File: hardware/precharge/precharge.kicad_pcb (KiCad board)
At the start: 2 copper layers, 111.8 x 81.3 mm, 109 parts, among them J1 Conn_01x02, J2 Conn_01x01, J3 Conn_01x02, J4 Conn_01x04, J5 Conn_01x03, J6 Conn_01x06, K2 G5Q-1EU DC12, K3 G5Q-1EU DC12, Q1 BC856, Q2 BC856, Q3 BC856, Q4 BC846, Q6 XP262N7002TR-G, Q7 XP262N7002TR-G, Q8 XP262N7002TR-G, U1 140817141410, U2 140817141410, U3 140817141410, U4 TLV274, U5 40106, U7 4013, U8 4071, U9 4013

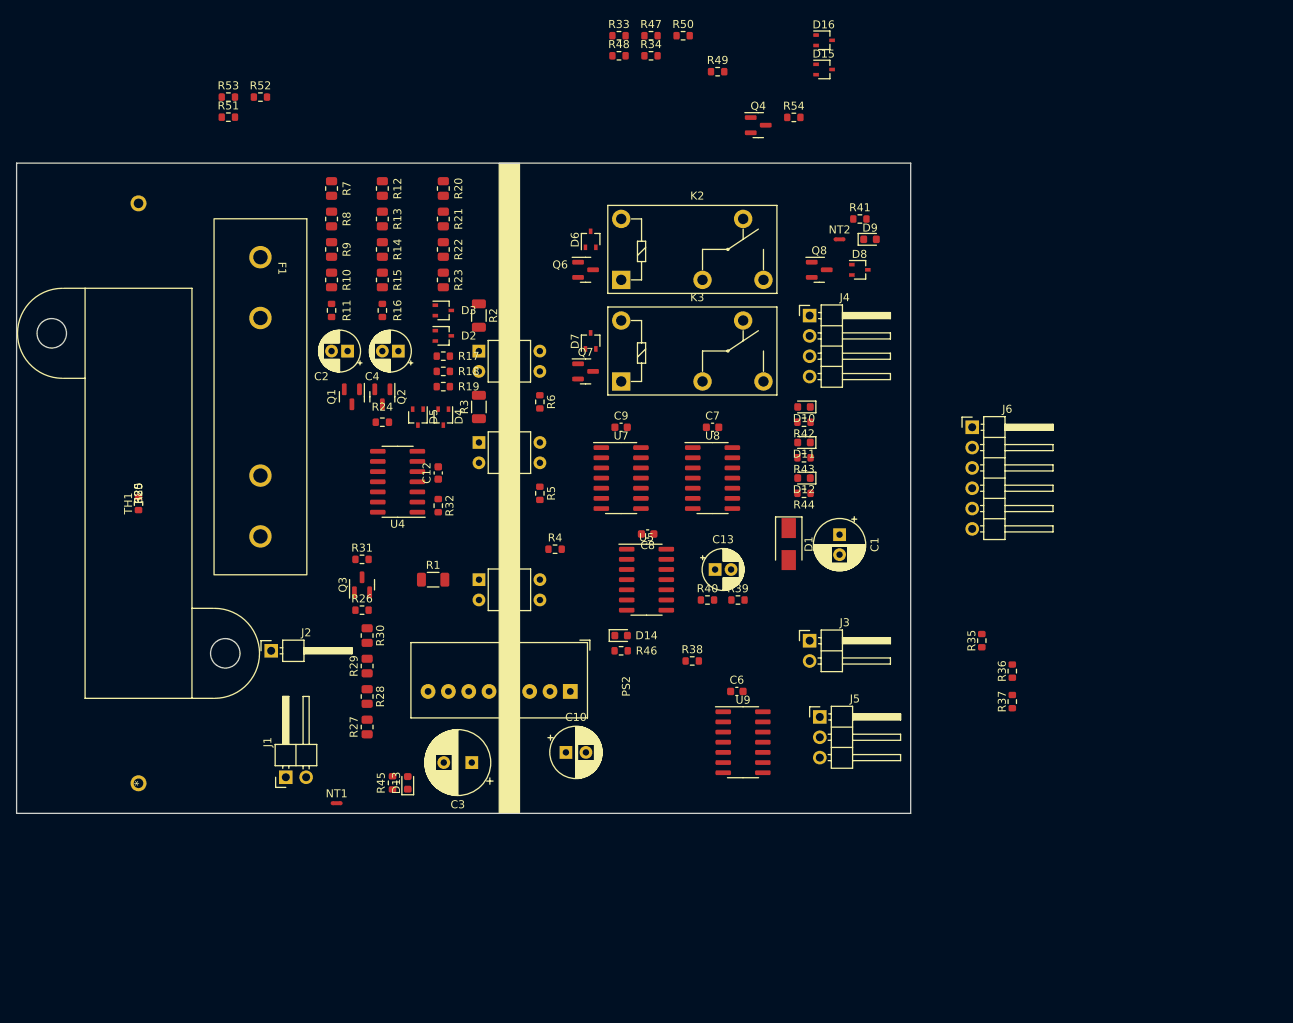
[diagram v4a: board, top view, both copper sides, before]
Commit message: Restarted PCB layout
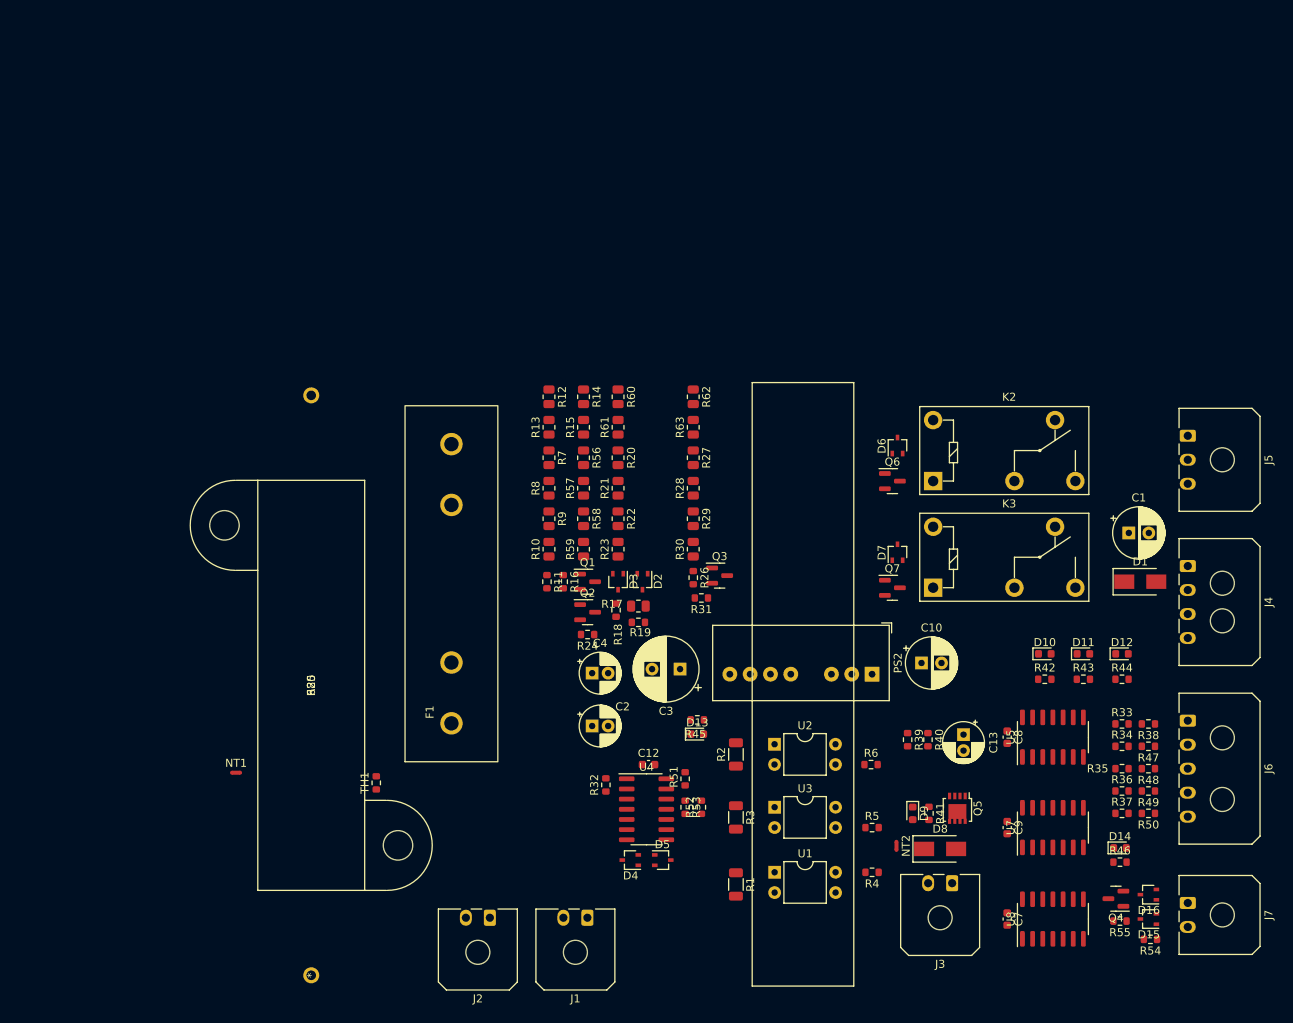
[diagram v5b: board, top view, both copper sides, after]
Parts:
- removed C6: 100n, Capacitor_SMD:C_0603_1608Metric
- removed Q8: XP262N7002TR-G, Package_TO_SOT_SMD:SOT-23
- removed U9: 4013, Package_SO:SOIC-14_3.9x8.7mm_P1.27mm
- added J7: Conn_01x02, Connector_Molex:Molex_Micro-Fit_3.0_43650-0200_1x02_P3.00mm_Horizontal, F.Cu at (256.9, 125.5)
- added Q5: BUK7M9R5-40H, Package_TO_SOT_SMD:LFPAK33, F.Cu at (228.1, 113.7)
- added R55: 10k, Resistor_SMD:R_0603_1608Metric, F.Cu at (248.4, 127.8)
- added R56: 453k, Resistor_SMD:R_0805_2012Metric, F.Cu at (181.4, 69.8)
- added R57: 453k, Resistor_SMD:R_0805_2012Metric, F.Cu at (181.4, 73.7)
- added R58: 453k, Resistor_SMD:R_0805_2012Metric, F.Cu at (181.4, 77.5)
- added R59: 453k, Resistor_SMD:R_0805_2012Metric, F.Cu at (181.4, 81.3)
- added R60: 453k, Resistor_SMD:R_0805_2012Metric, F.Cu at (185.7, 62.2)
- added R61: 453k, Resistor_SMD:R_0805_2012Metric, F.Cu at (185.7, 66.0)
- added R62: 453k, Resistor_SMD:R_0805_2012Metric, F.Cu at (195.1, 62.2)
- added R63: 453k, Resistor_SMD:R_0805_2012Metric, F.Cu at (195.1, 66.0)
- D8: value BAT54W -> SS14+; footprint Package_TO_SOT_SMD:SOT-323_SC-70 -> Diode_SMD:D_SMA
- J1, J3: footprint Connector_PinHeader_2.54mm:PinHeader_1x02_P2.54mm_Horizontal -> Connector_Molex:Molex_Micro-Fit_3.0_43650-0200_1x02_P3.00mm_Horizontal
- J2: value Conn_01x01 -> Conn_01x02; footprint Connector_PinHeader_2.54mm:PinHeader_1x01_P2.54mm_Horizontal -> Connector_Molex:Molex_Micro-Fit_3.0_43650-0200_1x02_P3.00mm_Horizontal
- J4: footprint Connector_PinHeader_2.54mm:PinHeader_1x04_P2.54mm_Horizontal -> Connector_Molex:Molex_Micro-Fit_3.0_43650-0400_1x04_P3.00mm_Horizontal
- J5: footprint Connector_PinHeader_2.54mm:PinHeader_1x03_P2.54mm_Horizontal -> Connector_Molex:Molex_Micro-Fit_3.0_43650-0300_1x03_P3.00mm_Horizontal
- J6: value Conn_01x06 -> Conn_01x05; footprint Connector_PinHeader_2.54mm:PinHeader_1x06_P2.54mm_Horizontal -> Connector_Molex:Molex_Micro-Fit_3.0_43650-0500_1x05_P3.00mm_Horizontal
- R10, R12, R13, R14, R15, R20, R21, R22, R27, R28, R29, R30, R7, R8, R9: value 680k -> 453k
- R17: value 120k -> 105k; footprint Resistor_SMD:R_0603_1608Metric -> Resistor_SMD:R_0805_2012Metric
- R18: value 1.5k -> 82
- R19: value 30k -> 31.6k
- R23: value 560k -> 348k
- moved D16 114.2 mm to (252.0, 124.5), turned to 180 degrees
- moved D15 113.7 mm to (252.0, 127.5), turned to 180 degrees
- moved R50 113.3 mm to (252.0, 114.3), turned to 180 degrees
- moved R54 112.0 mm to (252.2, 130.0), turned to 180 degrees
- moved R48 111.0 mm to (252.0, 108.7), turned to 180 degrees
- moved R47 108.4 mm to (252.0, 105.9), turned to 180 degrees
- moved R33 106.6 mm to (248.7, 103.1)
- moved Q4 106.5 mm to (247.9, 125.0), turned to 180 degrees
- moved R53 105.5 mm to (194.1, 113.5), turned to -90 degrees
- moved R49 104.8 mm to (252.0, 111.5), turned to 180 degrees
- moved R52 104.5 mm to (196.1, 113.5), turned to 90 degrees
- moved R34 104.5 mm to (248.7, 105.9)
- moved R51 100.5 mm to (194.1, 110.0), turned to -90 degrees
- moved NT2 76.2 mm to (220.5, 118.4), turned to -90 degrees
- moved R41 74.8 mm to (224.5, 114.3), turned to -90 degrees
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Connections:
- D8 pad 1: /RELAY- -> /LV side/RELAY+
- D8 pad 2: unconnected-(D8-Pad2) -> /LV side/RELAY-
- J3 pad 1: /RELAY- -> /LV side/RELAY-
- J5 pad 1: /RELAY- -> /LV side/PRECHARGE_ENABLED
- R14 pad 1: Net-(R13-Pad1) -> /HV side/HV_IN
- R15 pad 1: Net-(C4-Pad1) -> Net-(R15-Pad1)
- R20 pad 1: /HV side/HV_IN -> Net-(R20-Pad1)
- R27 pad 1: /HV side/TS+ -> Net-(R27-Pad1)
- R41 pad 2: /RELAY- -> /LV side/RELAY-
- R7 pad 1: /HV side/HV_IN -> Net-(R13-Pad1)
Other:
- board outline removed

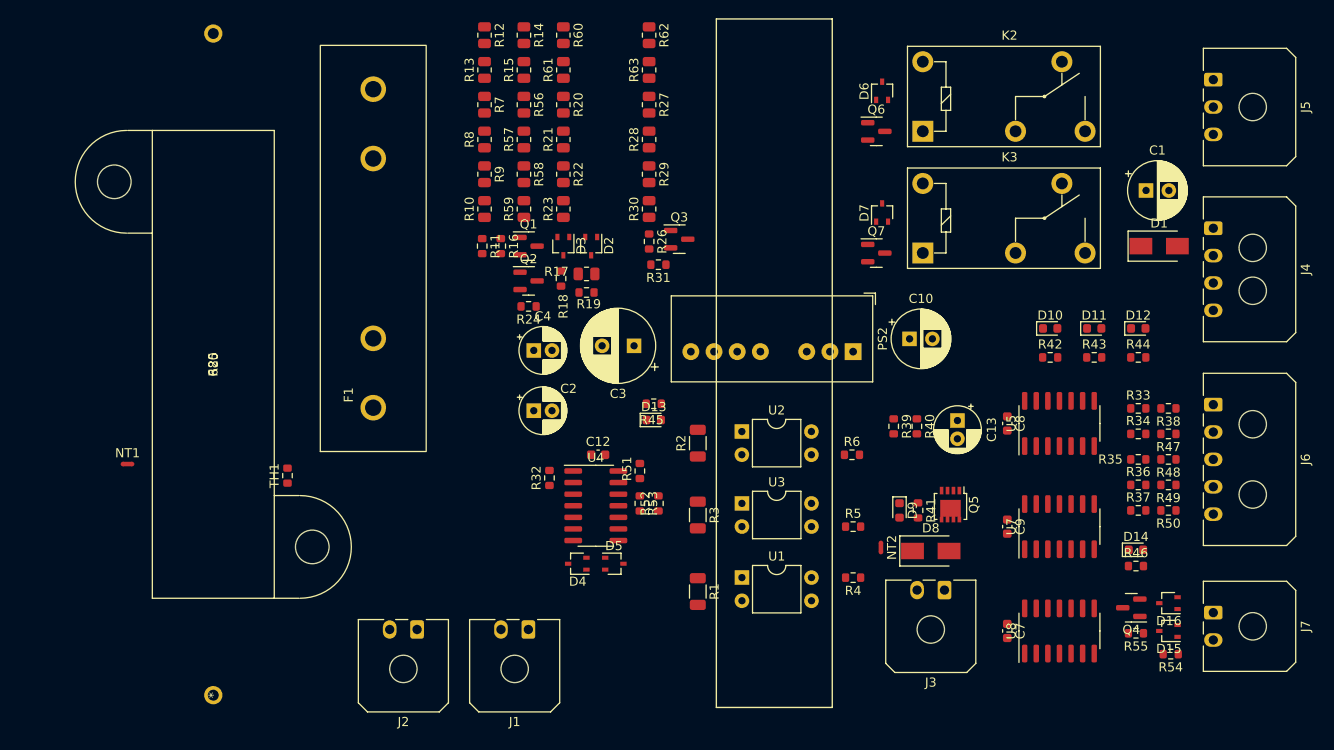
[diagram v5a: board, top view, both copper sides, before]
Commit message: Added precharge layout
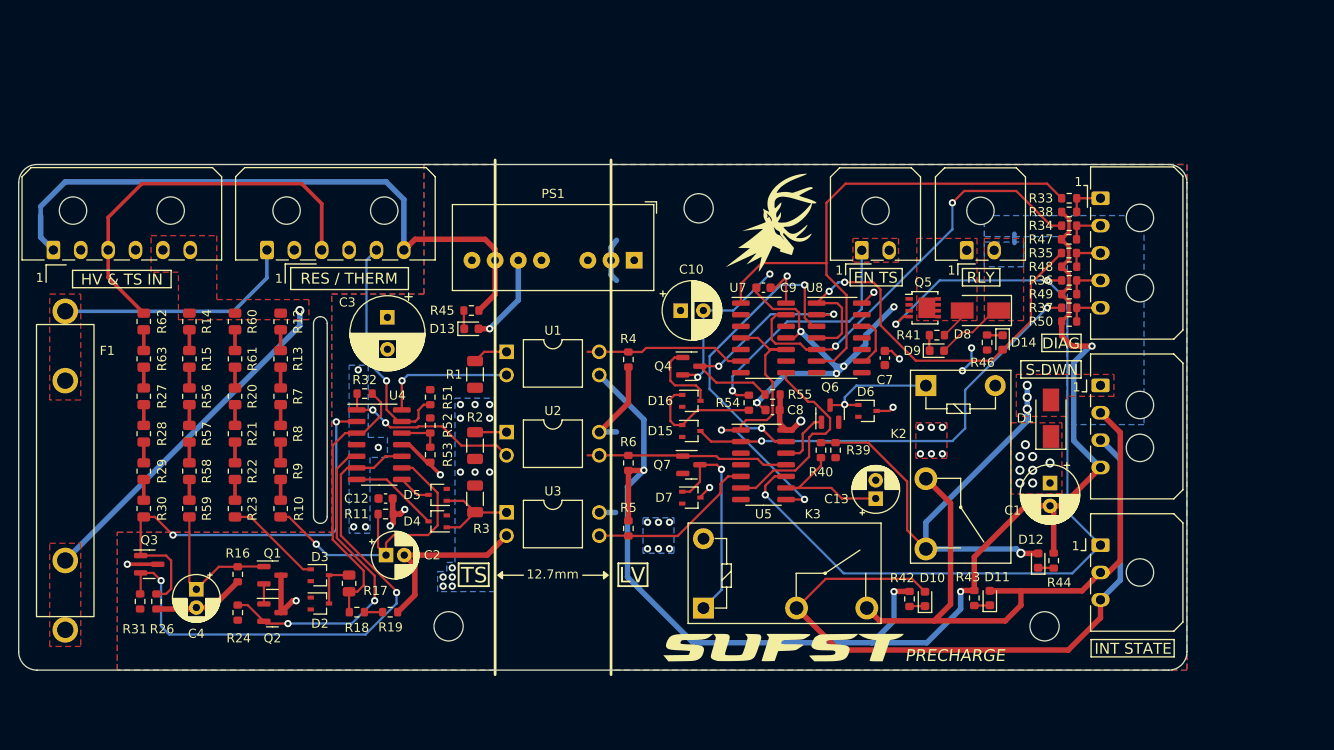
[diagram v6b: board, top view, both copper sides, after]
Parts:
- removed PS2: MPWF1212S-3W, footprints:MPWF1212S-3W
- removed R25: 680, footprints:HSA50680RJ
- removed TH1: NCU18WF104J60RB, Resistor_SMD:R_0603_1608Metric
- added G***: LOGO, footprints:sufst-text, F.Cu at (209.8, 129.3)
- added G***: LOGO, footprints:stag-logo, F.Cu at (208.4, 82.8)
- added H1: MountingHole, MountingHole:MountingHole_3.2mm_M3, F.Cu at (173.1, 127.0)
- added H2: MountingHole, MountingHole:MountingHole_3.2mm_M3, F.Cu at (200.5, 81.2)
- added H3: MountingHole, MountingHole:MountingHole_3.2mm_M3, F.Cu at (238.4, 127.0)
- added PS1: MPWF1212S-3W, footprints:MPWF1212S-3W, F.Cu at (193.4, 86.9)
- J1, J2: value Conn_01x02 -> Conn_01x06; footprint Connector_Molex:Molex_Micro-Fit_3.0_43650-0200_1x02_P3.00mm_Horizontal -> footprints:Molex_Micro-Fit_3.0_43650-0600_1x06_P3.00mm_Horizontal
- J3, J7: footprint Connector_Molex:Molex_Micro-Fit_3.0_43650-0200_1x02_P3.00mm_Horizontal -> footprints:Molex_Micro-Fit_3.0_43650-0200_1x02_P3.00mm_Horizontal
- J4: footprint Connector_Molex:Molex_Micro-Fit_3.0_43650-0400_1x04_P3.00mm_Horizontal -> footprints:Molex_Micro-Fit_3.0_43650-0400_1x04_P3.00mm_Horizontal
- J5: footprint Connector_Molex:Molex_Micro-Fit_3.0_43650-0300_1x03_P3.00mm_Horizontal -> footprints:Molex_Micro-Fit_3.0_43650-0300_1x03_P3.00mm_Horizontal
- J6: footprint Connector_Molex:Molex_Micro-Fit_3.0_43650-0500_1x05_P3.00mm_Horizontal -> footprints:Molex_Micro-Fit_3.0_43650-0500_1x05_P3.00mm_Horizontal
- K2, K3: footprint Relay_THT:Relay_SPDT_Omron-G5Q-1 -> footprints:PCH-112L2MH
- NT1, NT2: moved to B.Cu
- U1, U2, U3: footprint Package_DIP:DIP-4_W7.62mm -> footprints:DIP-4_W10.16mm
- moved Q3 68.1 mm to (140.3, 120.2)
- moved R31 67.7 mm to (139.3, 124.3), turned to 90 degrees
- moved R26 66.8 mm to (141.1, 124.3)
- moved R30 64.4 mm to (139.7, 114.1)
- moved R29 64.2 mm to (139.7, 110.0)
- moved R28 64.1 mm to (139.7, 105.9)
- moved R27 63.9 mm to (139.7, 101.8)
- moved R63 63.8 mm to (139.7, 97.7)
- moved R62 63.6 mm to (139.7, 93.6)
- moved J2 57.6 mm to (129.8, 85.8), turned to 0 degrees
- moved D16 56.8 mm to (199.7, 102.3), turned to 0 degrees
- moved D15 56.7 mm to (199.7, 105.6), turned to 0 degrees
- moved J7 55.3 mm to (218.4, 85.8), turned to 0 degrees
- moved Q4 55.0 mm to (199.7, 98.5), turned to 0 degrees
- moved R54 53.8 mm to (206.0, 102.5), turned to -90 degrees
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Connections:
- F1 pad 2: Net-(F1-Pad2) -> /HV side/RESISTOR_A
- J1 pad 1: /HV side/TS- -> /HV side/RESISTOR_A
- J1 pad 2: /HV side/TS+ -> unconnected-(J1-Pad2)
- J2 pad 1: /HV side/HV_IN -> /HV side/TS-
- J2 pad 2: /HV side/HV_IN -> unconnected-(J2-Pad2)
- R51 pad 2: Net-(R51-Pad2) -> /HV side/THERMOCOUPLE_SIG
- R62 pad 1: /HV side/TS+ -> /HV side/RESISTOR_B
- U4 pad 13: Net-(R51-Pad2) -> /HV side/THERMOCOUPLE_SIG
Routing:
- net GND: track 0.00 -> 147.3 mm, vias 0 -> 4
- net /HV_GND: track 0.00 -> 115.5 mm, vias 0 -> 5
- net /LV side/PRECHARGE_ENABLED: track 0.00 -> 98.7 mm, vias 0 -> 3
- net /LV side/SHUTDOWN_OUT_HIGH: track 0.00 -> 74.0 mm
- net /LV side/SHUTDOWN_OUT: track 0.00 -> 70.0 mm
- net /LV side/GND: track 0.00 -> 65.5 mm, vias 0 -> 15
- net Net-(Q3-Pad2): track 0.00 -> 61.7 mm, vias 0 -> 2
- net /LV side/OVERTEMP_FAULT_OUT: track 0.00 -> 60.4 mm
- net /LV side/SHUTDOWN_IN: track 0.00 -> 54.5 mm, vias 0 -> 4
- net /LV side/FAULT: track 0.00 -> 49.7 mm, vias 0 -> 2
- net Net-(Q3-Pad1): track 0.00 -> 49.1 mm, vias 0 -> 2
- net /LV side/AWAKE: track 0.00 -> 48.6 mm, vias 0 -> 2
- net /LV side/TIMING_FAULT_OUT: track 0.00 -> 46.7 mm, vias 0 -> 2
- net /HV side/RESISTOR_B: track 0.00 -> 43.0 mm
- net /HV side/HV_IN: track 0.00 -> 38.0 mm, vias 0 -> 1
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- added copper zone on B.Cu, net +12V
- added copper zone on F.Cu, net +12V
- added copper zone on F.Cu, net /HV side/HV_IN
- added copper zone on F.Cu, net /HV side/RESISTOR_A
- added copper zone on B.Cu, net /HV_+12V
- added copper zone on F.Cu, net /HV_+12V
- added copper zone on B.Cu, net /HV_GND
- added copper zone on F.Cu, net /LV side/ENABLE_TS
- added copper zone on B.Cu, net /LV side/GND
- added copper zone on F.Cu, net /LV side/GND
- added copper zone on B.Cu, net /LV side/RELAY+
- added copper zone on F.Cu, net /LV side/RELAY+
- added copper zone on F.Cu, net /LV side/RELAY-
- added copper zone on F.Cu, net /LV side/SHUTDOWN_IN
- added copper zone on B.Cu, net /LV side/SHUTDOWN_OUT
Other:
- board outline added: 128 x 55.4 mm
- board text added: "1"
- board text added: "12.7mm"
- board text added: "AWAKE"
- board text added: "DIAG"
- board text added: "EN TS"
- board text added: "FAULT"
- board text added: "GND"
- board text added: "HV & TS IN"
- board text added: "HV GND"
- board text added: "HV IN"
- board text added: "INT STATE"
- board text added: "LV"
- board text added: "NC"
- board text added: "OVERTEMP"
- board text added: "PRE CHRG EN"
- board text added: "PRECHARGE"
- board text added: "RES / THERM"
- board text added: "RES A"
- board text added: "RES B"
- board text added: "RLY"
- board text added: "S-DWN"
- board text added: "SHT DWN IN"
- board text added: "SHT DWN OUT"
- board text added: "SHT DWN OUT HI"
- board text added: "THERMO SIG"
- board text added: "TIMING"
- board text added: "TS"
- board text added: "TS-"

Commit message: Added initial indicator light
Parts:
- added D17: BZX84C12L, Package_TO_SOT_SMD:SOT-23, F.Cu at (147.3, 153.9)
- added D18: BZX84C6V2L, Package_TO_SOT_SMD:SOT-23, F.Cu at (162.7, 141.9)
- added J8: LED, footprints:Molex_Micro-Fit_3.0_43650-0200_1x02_P3.00mm_Horizontal, F.Cu at (152.9, 149.7)
- added Q8: FQD1N80TM, Package_TO_SOT_SMD:TO-252-2, F.Cu at (142.5, 143.8)
- added Q9: XP262N7002TR-G, Package_TO_SOT_SMD:SOT-23, F.Cu at (138.8, 156.4)
- added R25: 200k, Resistor_SMD:R_0805_2012Metric, F.Cu at (151.9, 153.2)
- added R64: 200k, Resistor_SMD:R_0805_2012Metric, F.Cu at (162.4, 145.7)
- added R65: 200k, Resistor_SMD:R_0805_2012Metric, F.Cu at (151.9, 156.1)
- added R66: 200k, Resistor_SMD:R_0805_2012Metric, F.Cu at (143.5, 157.6)
- added R67: 200k, Resistor_SMD:R_0805_2012Metric, F.Cu at (167.3, 141.2)
- added R68: 470, Resistor_SMD:R_0603_1608Metric, F.Cu at (156.2, 152.9)
- added R69: 900k, Resistor_SMD:R_0603_1608Metric, F.Cu at (166.7, 145.4)
- added R70: 110k, Resistor_SMD:R_0603_1608Metric, F.Cu at (162.2, 148.4)
- added R71: 4.7k, Resistor_SMD:R_0603_1608Metric, F.Cu at (147.7, 157.4)
- added U6: OP777, Package_SO:SOIC-8_3.9x4.9mm_P1.27mm, F.Cu at (140.6, 151.0)

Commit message: Latest precharge updates
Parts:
- D17: value BZX84C12L -> MMSZ4699T1G; footprint Package_TO_SOT_SMD:SOT-23 -> Diode_SMD:D_SOD-123
- D18: value BZX84C6V2L -> MMSZ4691T1G; footprint Package_TO_SOT_SMD:SOT-23 -> Diode_SMD:D_SOD-123
- PS1: value MPWF1212S-3W -> 0.5S7B_1212S3UP; footprint footprints:MPWF1212S-3W -> footprints:0.5S7B_1212S3UP
- moved R25 62.0 mm to (134.7, 93.6), turned to 90 degrees
- moved R65 57.0 mm to (134.7, 101.8), turned to 90 degrees
- moved R64 55.4 mm to (134.7, 97.7), turned to -90 degrees
- moved R66 52.4 mm to (134.7, 105.9), turned to -90 degrees
- moved R67 45.2 mm to (134.7, 110.0), turned to 90 degrees
- moved R69 29.5 mm to (137.2, 143.4), turned to -90 degrees
- moved D18 29.4 mm to (133.3, 142.6), turned to -90 degrees
- moved R68 27.8 mm to (133.5, 136.8), turned to 180 degrees
- moved R70 27.2 mm to (135.5, 143.4), turned to 90 degrees
- moved J8 25.3 mm to (129.5, 139.8), turned to 90 degrees
- moved R71 20.2 mm to (137.2, 140.2), turned to 90 degrees
- moved D17 20.0 mm to (144.2, 134.1), turned to 180 degrees
- moved Q9 16.4 mm to (148.9, 143.5)
- moved Q8 12.8 mm to (153.0, 136.4)
- moved U6 9.24 mm to (142.4, 141.9)
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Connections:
- D17 pad 1: /Indicator Light/TS- -> Net-(D17-Pad1)
- D17 pad 2: unconnected-(D17-Pad2) -> /HV side/TS-
- D18 pad 1: /Indicator Light/TS- -> Net-(D18-Pad1)
- D18 pad 2: unconnected-(D18-Pad2) -> /HV side/TS-
- PS1 pad 1: /LV side/GND -> +12V
- PS1 pad 2: +12V -> /LV side/GND
- PS1 pad 5: (no net) -> /HV_GND
- PS1 pad 7: /HV_GND -> /HV_+12V
- Q8 pad 1: Net-(D17-Pad3) -> Net-(D17-Pad1)
- Q8 pad 2: /Indicator Light/TS+ -> /HV side/RESISTOR_B
- Q9 pad 2: /Indicator Light/TS- -> /HV side/TS-
- R25 pad 2: /Indicator Light/TS+ -> /HV side/RESISTOR_B
- R67 pad 1: Net-(D17-Pad3) -> Net-(D17-Pad1)
- R69 pad 2: /Indicator Light/TS+ -> /HV side/RESISTOR_B
- R70 pad 1: /Indicator Light/TS- -> /HV side/TS-
- R71 pad 1: Net-(D18-Pad3) -> Net-(D18-Pad1)
- U6 pad 2: Net-(D18-Pad3) -> Net-(D18-Pad1)
- U6 pad 4: /Indicator Light/TS- -> /HV side/TS-
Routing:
- net /HV side/TS-: track 4.35 -> 67.5 mm, vias 0 -> 2
- net /HV side/RESISTOR_B: track 43.0 -> 94.5 mm, vias 0 -> 3
- net Net-(D17-Pad1): track 0.00 -> 35.0 mm
- net Net-(Q9-Pad3): track 0.00 -> 23.0 mm
- net Net-(J8-Pad1): track 0.00 -> 22.0 mm
- net /HV_+12V: track 10.0 -> 0.00 mm, vias 18 -> 17
- net /LV side/GND: track 65.5 -> 74.2 mm
- net /HV side/RESISTOR_A: track 26.7 -> 33.5 mm
- net /HV side/HV_IN: track 38.0 -> 44.8 mm
- net Net-(D18-Pad1): track 0.00 -> 6.76 mm
- net +12V: track 35.8 -> 30.9 mm
- net Net-(R69-Pad1): track 0.00 -> 4.40 mm
- net Net-(Q9-Pad1): track 0.00 -> 3.15 mm
- net Net-(J8-Pad2): track 0.00 -> 3.11 mm
- net Net-(R66-Pad2): track 0.00 -> 2.28 mm
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- added copper zone on B.Cu, net /HV side/RESISTOR_B
- added copper zone on F.Cu, net /HV side/TS-
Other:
- board size 128 x 55.4 mm -> 133.9 x 70.9 mm
- board text added: "AIL"
